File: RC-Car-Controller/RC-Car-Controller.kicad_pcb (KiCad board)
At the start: 4 copper layers, 138.8 x 77 mm, 114 parts, among them J1 Conn_01x02, J2 2171790001, J3 MCU_IF, J4 RF_IF, J5 ANT_IF, J6 Conn_01x08_Pin, Q1 DMG2301L, SW1 SW_Push, SW2 SW_SPDT, SW3 1825027-8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

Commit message: Finished prelim. Car and added screw holes
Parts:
- added REF**: Overtime_Large, _LOGOS:Overtime_Large, F.Cu at (115.1, 111.9)
- added REF**: MountingHole_3.2mm_M3, MountingHole:MountingHole_3.2mm_M3, F.Cu at (95.6, 91.8)
- added REF**: MountingHole_3.2mm_M3, MountingHole:MountingHole_3.2mm_M3, F.Cu at (182.4, 102.9)
- added REF**: MountingHole_3.2mm_M3, MountingHole:MountingHole_3.2mm_M3, F.Cu at (95.6, 54.2)
- added REF**: MountingHole_3.2mm_M3, MountingHole:MountingHole_3.2mm_M3, F.Cu at (204.0, 54.2)
- added REF**: MountingHole_3.2mm_M3, MountingHole:MountingHole_3.2mm_M3, F.Cu at (204.0, 91.8)
- added REF**: MountingHole_3.2mm_M3, MountingHole:MountingHole_3.2mm_M3, F.Cu at (117.9, 102.9)
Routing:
- net /Inputs/Button_L: track 93.5 -> 90.1 mm, vias 0 -> 1
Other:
- board text added: "50Ω"

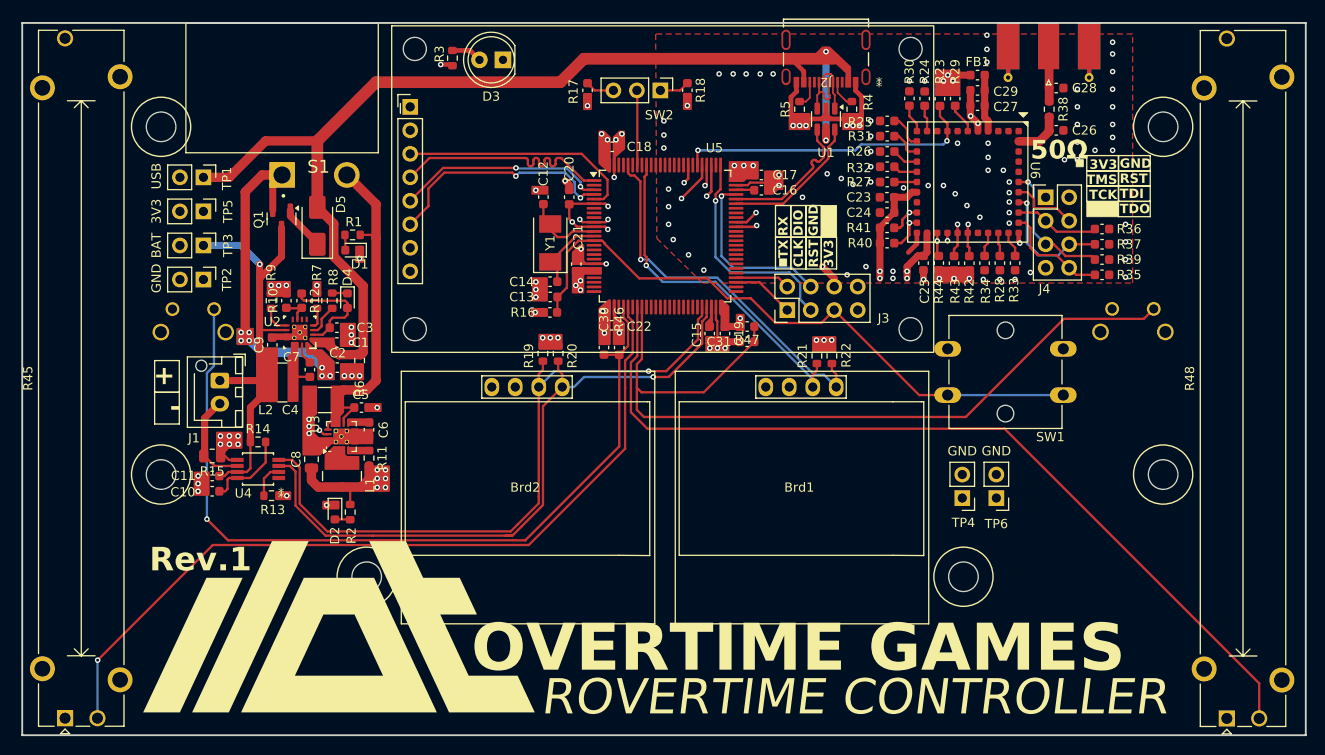
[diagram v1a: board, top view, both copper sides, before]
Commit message: Finished BOM Drafts
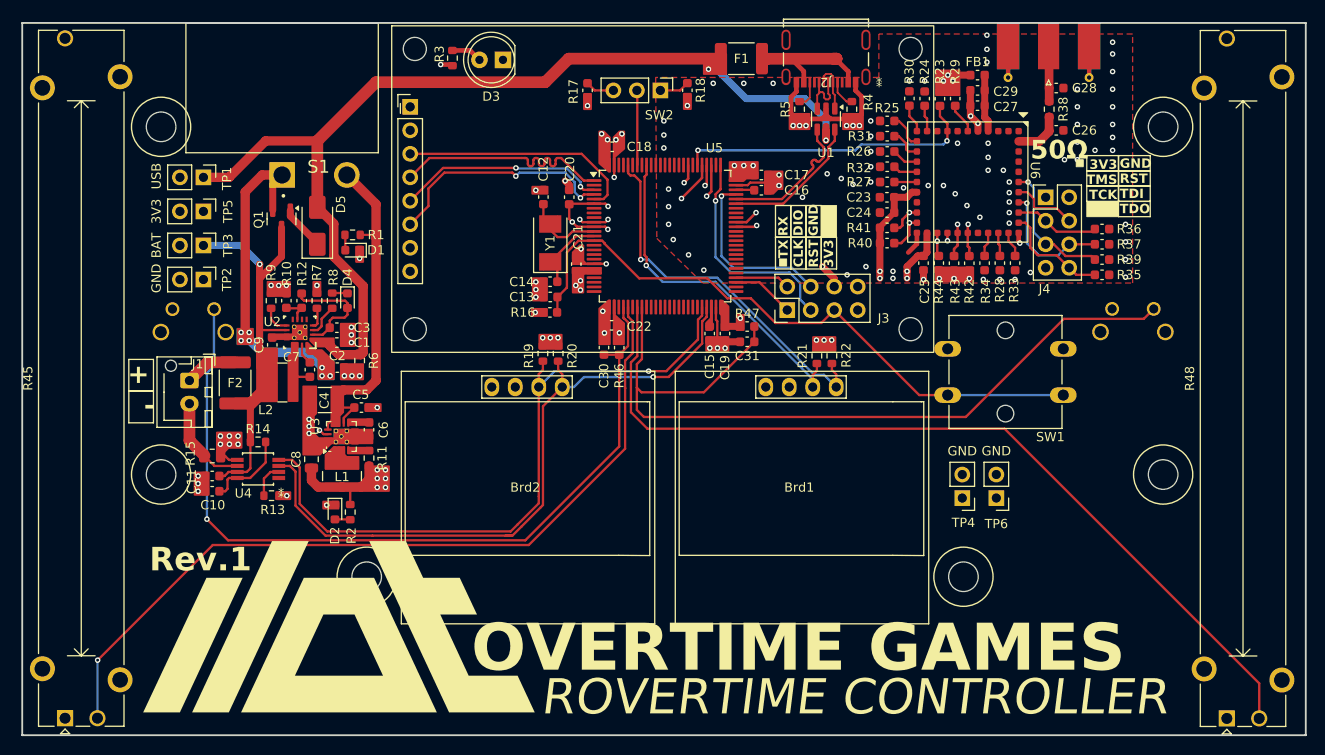
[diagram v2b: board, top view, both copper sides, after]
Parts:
- added F1: 3A Hold, Fuse:Fuse_1812_4532Metric_Pad1.30x3.40mm_HandSolder, F.Cu at (158.4, 46.9)
- added F2: 3A Hold, Fuse:Fuse_1812_4532Metric_Pad1.30x3.40mm_HandSolder, F.Cu at (103.6, 81.9)
- C1: value 2.2uF/16V -> 2.2uF/10V
- C10: value 220nF/16V -> 0.22uF/10V
- C11: value 1uF/16V -> 1uF/10V
- C24, C25, C29: value 100nF/10V -> 0.1uF/10V
- C30, C31: value 0.22uF/10V -> 0.1uF/10V
- R3: value 60ohm -> 220ohm
- R46, R47: value 10k -> 10kohm
- R7: value 20kohm -> 13kohm
- moved J1 3.28 mm to (98.7, 81.7)
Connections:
- J1 pad 1: VDD_BATT -> Net-(J1-Pin_1)
- J2 pad A4/B9: VDD_USB -> Net-(F1-Pad2)
- J2 pad B4/A9: VDD_USB -> Net-(F1-Pad2)
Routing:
- net Net-(F1-Pad2): track 0.00 -> 13.7 mm
- net VDD_USB: track 118.0 -> 110.4 mm
- net Net-(J1-Pin_1): track 0.00 -> 5.75 mm
- net VDD_BATT: track 46.5 -> 45.8 mm
- net GNDA: vias 128 -> 126

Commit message: Finished Rev1
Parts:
- D5: value SK36A-LTP -> SK54A-LTP
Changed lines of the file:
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@@
 			)
 		)
-		(property "Value" "SK36A-LTP"
+		(property "Value" "SK54A-LTP"
 			(at 0 2.6 90)
 			(layer "F.Fab")
@@
 			)
 		)
-		(property "MANUF_PN" "SK36A-LTP"
+		(property "MANUF_PN" "SK54A-LTP"
 			(at 0 0 90)
 			(unlocked yes)

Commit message: Fixed Models
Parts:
- R45, R48: footprint Potentiometer_THT:Potentiometer_Bourns_PTA6043_Single_Slide -> PTA6043-2015CPB103:PTA6043-2015CPB103
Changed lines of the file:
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@@
 		)
 	)
-	(footprint "Potentiometer_THT:Potentiometer_Bourns_PTA6043_Single_Slide"
+	(footprint "PTA6043-2015CPB103:PTA6043-2015CPB103"
 		(layer "F.Cu")
 		(at 85.25 118.164 90)
@@
 			)
 		)
-		(property "Footprint" "Potentiometer_THT:Potentiometer_Bourns_PTA6043_Single_Slide"
+		(property "Footprint" "PTA6043-2015CPB103:PTA6043-2015CPB103"
 			(at 0 0 90)
 			(unlocked yes)
@@
 			)
 		)
+		(model "D:/8_Tank_MINI/Electronics/RC-Car-PCB/RC-Car-PCB/Libraries/PTA6043-2015CPB103/PTA6043-2015CPB103.step"
+			(offset
+				(xyz 36.7 -1.8 0)
+			)
+			(scale
+				(xyz 1 1 1)
+			)
+			(rotate
+				(xyz -90 0 0)
+			)
+		)
 	)
 	(footprint "Capacitor_SMD:C_0603_1608Metric"
@@
 			(solder_mask_margin 0.102)
 		)
+		(model "D:/8_Tank_MINI/Electronics/RC-Car-PCB/RC-Car-PCB/Libraries/R1966ABLKBLKGR/R1966ABLKBLKGR.step"
+			(offset
+				(xyz 0 0 -1)
+			)
+			(scale
+				(xyz 1 1 1)
+			)
+			(rotate
+				(xyz -90 0 0)
+			)
+		)
 	)
 	(footprint "Capacitor_SMD:C_0603_1608Metric"
@@
 		)
 	)
-	(footprint "Potentiometer_THT:Potentiometer_Bourns_PTA6043_Single_Slide"
+	(footprint "PTA6043-2015CPB103:PTA6043-2015CPB103"
 		(layer "F.Cu")
 		(at 210.848 118.188 90)
@@
 			)
 		)
-		(property "Footprint" "Potentiometer_THT:Potentiometer_Bourns_PTA6043_Single_Slide"
+		(property "Footprint" "PTA6043-2015CPB103:PTA6043-2015CPB103"
 			(at 0 0 90)
 			(unlocked yes)
@@
 			)
 		)
+		(model "D:/8_Tank_MINI/Electronics/RC-Car-PCB/RC-Car-PCB/Libraries/PTA6043-2015CPB103/PTA6043-2015CPB103.step"
+			(offset
+				(xyz 36.7 -1.8 0)
+			)
+			(scale
+				(xyz 1 1 1)
+			)
+			(rotate
+				(xyz -90 0 0)
+			)
+		)
 	)
 	(footprint "Connector_PinHeader_2.54mm:PinHeader_1x02_P2.54mm_Vertical"
@@
 			(pintype "bidirectional+no_connect")
 		)
+		(model "D:/8_Tank_MINI/Electronics/RC-Car-PCB/RC-Car-PCB/Libraries/USB-C 2171790001/2171790001.STEP"
+			(offset
+				(xyz 0 -0.1 0)
+			)
+			(scale
+				(xyz 1 1 1)
+			)
+			(rotate
+				(xyz -90 0 0)
+			)
+		)
 	)
 	(footprint "Connector_PinHeader_2.54mm:PinHeader_1x02_P2.54mm_Vertical"
@@
 		)
 		(fp_text user "*"
-			(at -1.778 0 0)
+			(at -1.778 0 180)
+			(unlocked yes)
 			(layer "B.SilkS")
 			(effects
@@
 		)
 		(fp_text user "*"
-			(at 1.27 0 0)
+			(at 1.27 0 180)
+			(unlocked yes)
 			(layer "B.Fab")
 			(effects
@@
 			)
 		)
-		(fp_text user "*"
-			(at 1.27 0 180)
+		(fp_text user "${REFERENCE}"
+			(at 2.250001 3.260899 180)
 			(unlocked yes)
 			(layer "B.Fab")
@@
 			)
 		)
-		(fp_text user "${REFERENCE}"
-			(at 2.250001 3.260899 180)
+		(fp_text user "*"
+			(at 1.27 0 180)
 			(unlocked yes)
 			(layer "B.Fab")
@@
 			(pintype "unspecified")
 		)
+		(model "D:/8_Tank_MINI/Electronics/RC-Car-PCB/RC-Car-PCB/Libraries/SW2_1825027-C_TEC/c-1825027-8-g-3d.stp"
+			(offset
+				(xyz 2.4 -2.6 4)
+			)
+			(scale
+				(xyz 1 1 1)
+			)
+			(rotate
+				(xyz -90 0 0)
+			)
+		)
 	)
 	(footprint "SW2_1825027-C_TEC:SW2_1825027-C_TEC"
@@
 		)
 		(fp_text user "*"
-			(at -1.778 0 0)
+			(at -1.778 0 180)
+			(unlocked yes)
 			(layer "B.SilkS")
 			(effects
@@
 			)
 		)
-		(fp_text user "${REFERENCE}"
-			(at 2.250001 3.260899 180)
-			(unlocked yes)
+		(fp_text user "*"
+			(at 1.27 0 0)
 			(layer "B.Fab")
 			(effects
@@
 			)
 		)
-		(fp_text user "*"
-			(at 1.27 0 0)
+		(fp_text user "${REFERENCE}"
+			(at 2.250001 3.260899 180)
+			(unlocked yes)
 			(layer "B.Fab")
 			(effects
@@
 			(pintype "unspecified")
 		)
+		(model "D:/8_Tank_MINI/Electronics/RC-Car-PCB/RC-Car-PCB/Libraries/SW2_1825027-C_TEC/c-1825027-8-g-3d.stp"
+			(offset
+				(xyz 2.4 -2.6 4)
+			)
+			(scale
+				(xyz 1 1 1)
+			)
+			(rotate
+				(xyz -90 0 0)
+			)
+		)
 	)
